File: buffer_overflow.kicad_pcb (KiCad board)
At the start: 2 copper layers, 52 x 107 mm, 27 parts, among them J1 Barrel_Jack_Switch, J3 NRJ4HF, J4 NRJ4HF, U1 LM741

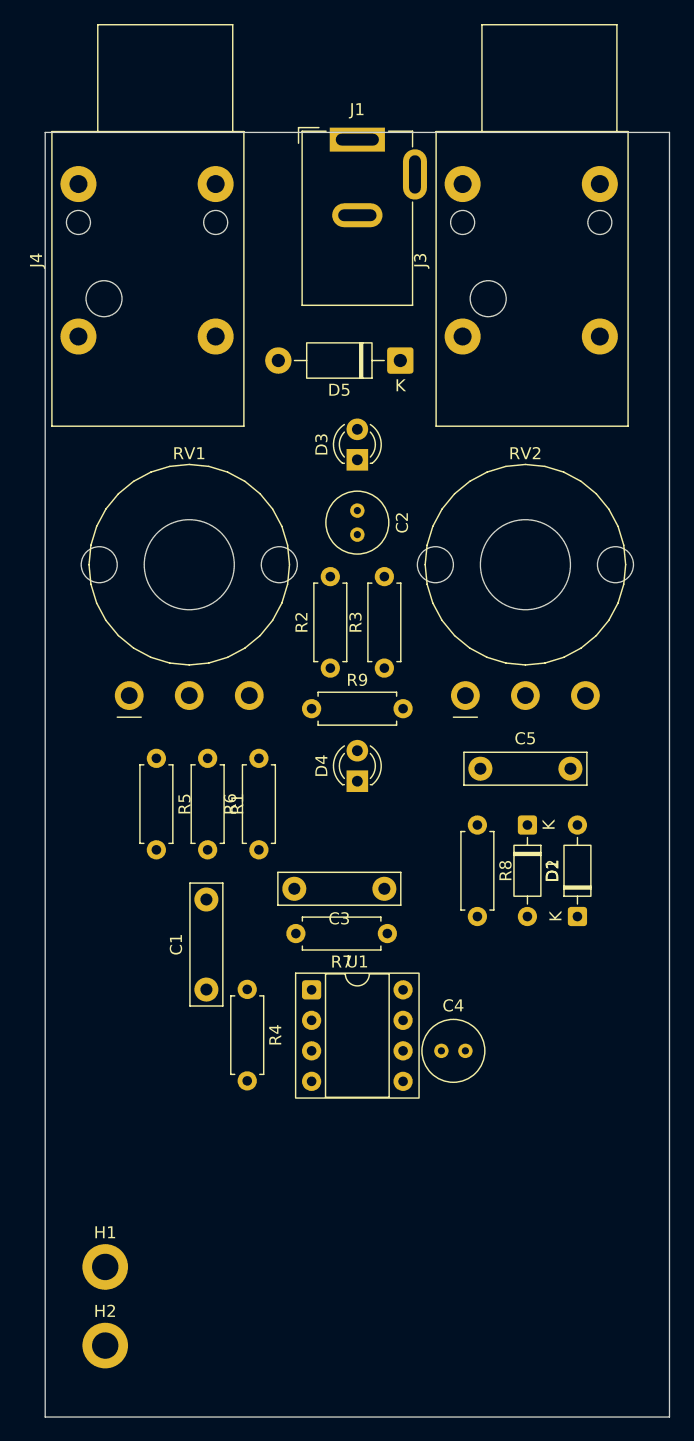
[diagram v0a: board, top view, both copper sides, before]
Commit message: Add Power/LED netclasses and update board
Net classes (Board Setup):
- Power (32 mil): /9V0, /AGND, /PGND, /BAT_GND
- LED (24 mil): /LED*
- Default (14 mil): all other signal nets

Includes accompanying schematic and PCB edits.

Co-Authored-By: Claude Opus 4.8 (1M context) <noreply@anthropic.com>
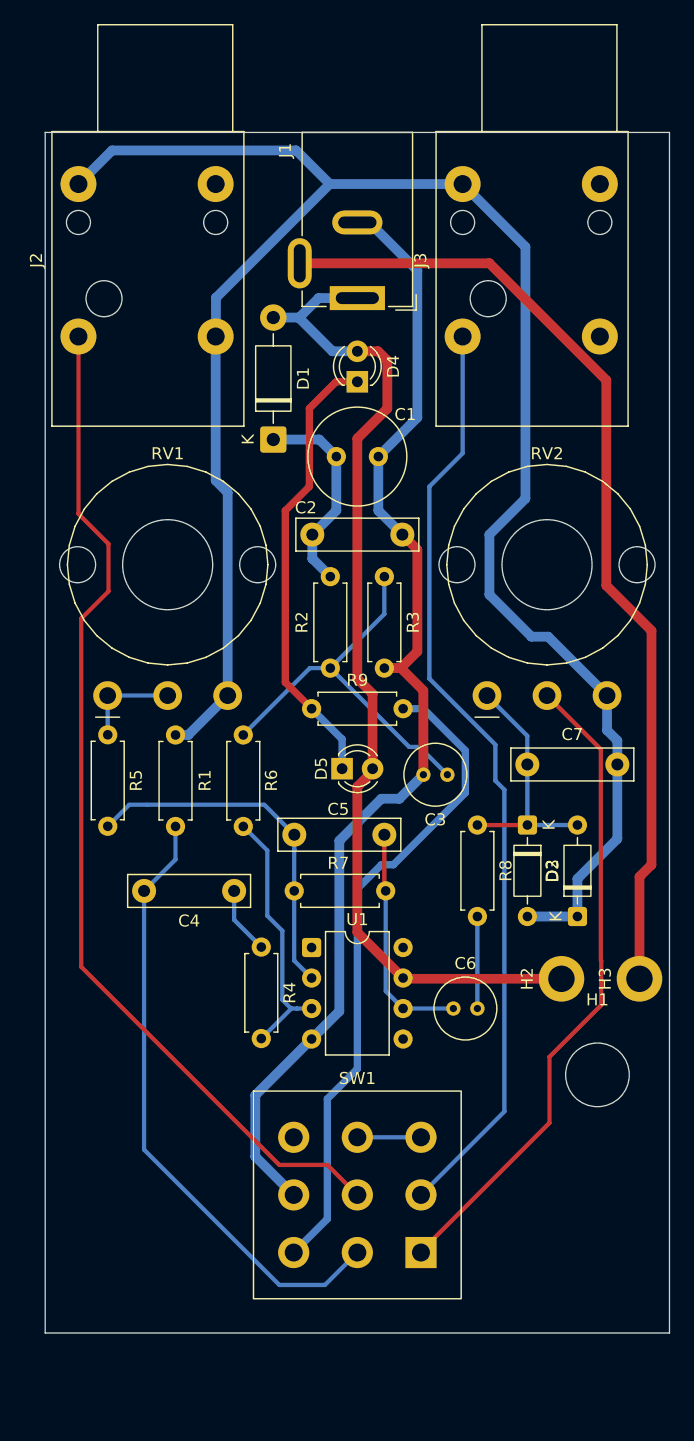
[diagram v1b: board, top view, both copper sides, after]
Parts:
- removed the D5 at (134.1, 78.5)
- added C1: 100uF, Capacitor_THT:C_Radial_D8.0mm_H11.5mm_P3.50mm, F.Cu at (128.8, 86.5)
- added C2: 100nF, Capacitor_THT:C_Rect_L10.0mm_W2.5mm_P7.50mm_MKS4, F.Cu at (126.8, 93.0)
- added D1: 1N4001, Diode_THT:D_DO-41_SOD81_P10.16mm_Horizontal, F.Cu at (123.5, 85.1)
- added H1: MountingHole, MountingHole:MountingHole_5.3mm_M5, F.Cu at (150.5, 138.0)
- added SW1: SW_FSW800_3PDT, edaFactory:SW_FSW800_3PDT, F.Cu at (130.5, 148.0)
- C3: renamed from C2; value C_US -> 10uF
- J2: renamed from J4; value NRJ4HF -> NRJ4HF-1
- U1: value LM741 -> TL071; footprint Package_DIP:DIP-8_W7.62mm_Socket -> Package_DIP:DIP-8_W7.62mm
- moved H3 54.0 mm to (154.0, 130.0), turned to 90 degrees
- moved H2 44.9 mm to (147.5, 130.0), turned to 90 degrees
- moved C3 23.2 mm to (138.0, 113.0), turned to 180 degrees
- moved J1 13.2 mm to (130.5, 73.3), turned to 180 degrees
- moved C4 8.53 mm to (120.2, 122.7), turned to 180 degrees
- moved D4 6.50 mm to (130.5, 80.3)
- moved R5 4.50 mm to (109.7, 109.7)
- moved C5 4.50 mm to (132.8, 118.0)
- moved C7 3.92 mm to (144.7, 112.1)
- moved R4 3.71 mm to (122.5, 127.4)
- moved C6 3.66 mm to (138.5, 132.5)
- moved R7 3.56 mm to (132.9, 122.7)
- moved U1 3.52 mm to (126.7, 127.4)
- moved R1 3.31 mm to (115.4, 109.7)
- moved R6 2.34 mm to (121.0, 117.3)
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- renumbered C1 to C4, C3 to C5, C4 to C6, C5 to C7, D1 to D2, D2 to D3, D3 to D4, D4 to D5, H1 to H2, H2 to H3
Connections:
- net /741_Inv renamed /INV
- net /741_OUT renamed /OPAMPOUT
- net Net-(H2-Pad1) renamed /BAT_GND
- net Net-(U1-+) renamed /NINV
- C4 pad 2: /EFFECT_IN -> /CIRCIN
- D4 pad 1: unconnected-(D3-K-Pad1) -> /LEDK
- D4 pad 2: Net-(D3-A) -> /9V0
- D5 pad 1: unconnected-(D4-K-Pad1) -> /LEDK
- D5 pad 2: unconnected-(D4-A-Pad2) -> /9V0
- J2 pad S: /EFFECT_IN -> /AGND
- J2 pad SN: /AGND -> unconnected-(J2-PadSN)
- J2 pad T: /AGND -> /INPUT_TIP
- J2 pad TN: unconnected-(J4-PadTN) -> /AGND
- J3 pad S: /EFFECT_OUT -> /AGND
- J3 pad T: /AGND -> /OUT_TIP
- R1 pad 2: /EFFECT_IN -> /CIRCIN
- R9 pad 1: unconnected-(R9-Pad1) -> /LEDK
- R9 pad 2: Net-(D3-A) -> /LEDA
- RV2 pad 2: /EFFECT_OUT -> /CIRCOUT
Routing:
- net /AGND: track 0.00 -> 162.2 mm
- net /PGND: track 0.00 -> 97.1 mm
- net /INPUT_TIP: track 0.00 -> 85.3 mm
- net /9V0: track 0.00 -> 84.8 mm
- net /BAT_GND: track 0.00 -> 81.4 mm
- net /OUT_TIP: track 0.00 -> 78.1 mm
- net /LEDA: track 0.00 -> 54.9 mm
- net /CIRCOUT: track 0.00 -> 54.5 mm
- net /CIRCIN: track 0.00 -> 51.6 mm
- net /LEDK: track 0.00 -> 37.7 mm
- net /VREF: track 0.00 -> 32.5 mm
- net /INV: track 0.00 -> 28.9 mm
- net /NINV: track 0.00 -> 22.1 mm
- net /PRE_VOLUME: track 0.00 -> 20.5 mm
- net /OPAMPOUT: track 0.00 -> 19.3 mm
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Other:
- board size 52 x 107 mm -> 52 x 100 mm

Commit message: Add /VREF to Power netclass and route board
Co-Authored-By: Claude Opus 4.8 (1M context) <noreply@anthropic.com>
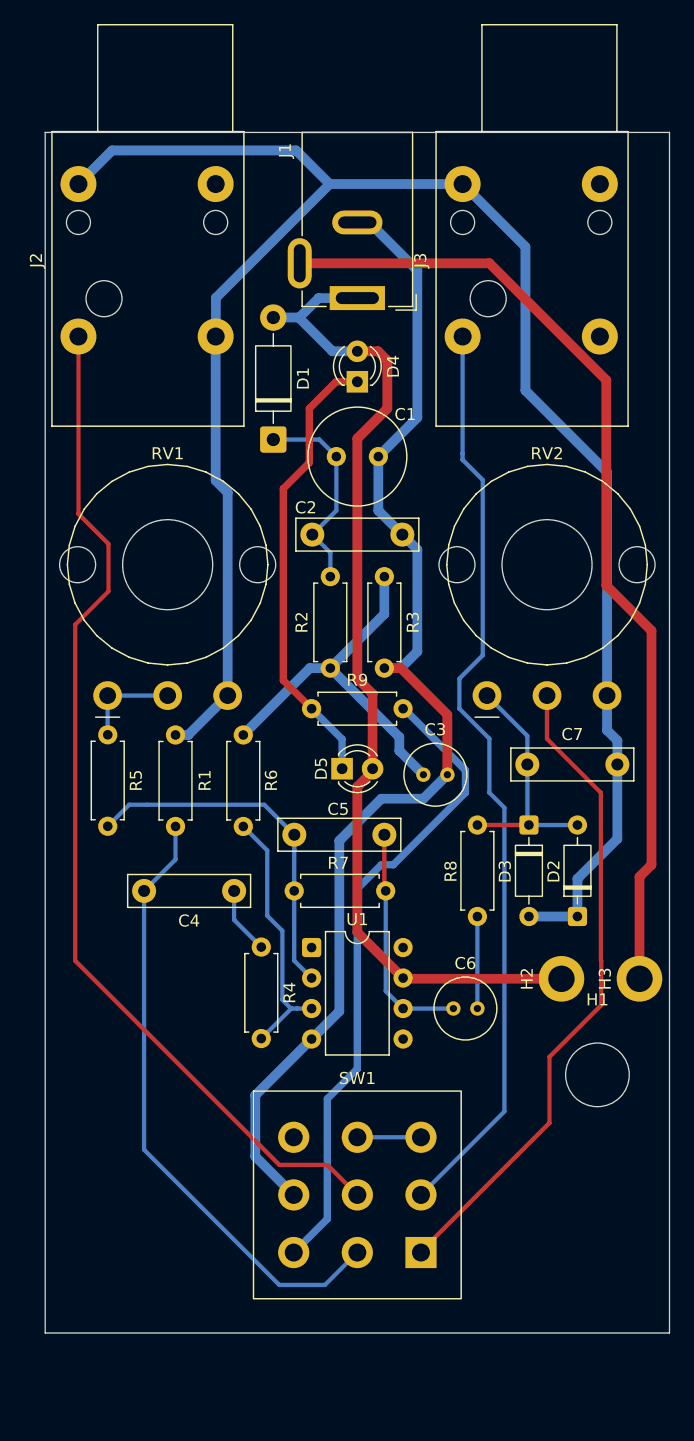
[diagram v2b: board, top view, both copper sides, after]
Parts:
- moved C3 2.00 mm to (136.0, 113.0), turned to 0 degrees
- moved D3 0.13 mm to (144.8, 117.2)
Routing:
- net /PGND: track 97.1 -> 101.3 mm
- net /AGND: track 162.2 -> 158.7 mm
- net /VREF: track 32.5 -> 31.1 mm
- net /LEDA: track 54.9 -> 54.0 mm
- net /OUT_TIP: track 78.1 -> 77.4 mm

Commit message: Add back-silkscreen contact/credit text
Co-Authored-By: Claude Opus 4.8 (1M context) <noreply@anthropic.com>
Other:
- board text added: "DAVID SHUMAN"
- board text added: "DOD OD-250"
- board text added: "davidshuman@gmail.com hardware & software analog - digital - audio tube amplifiers"

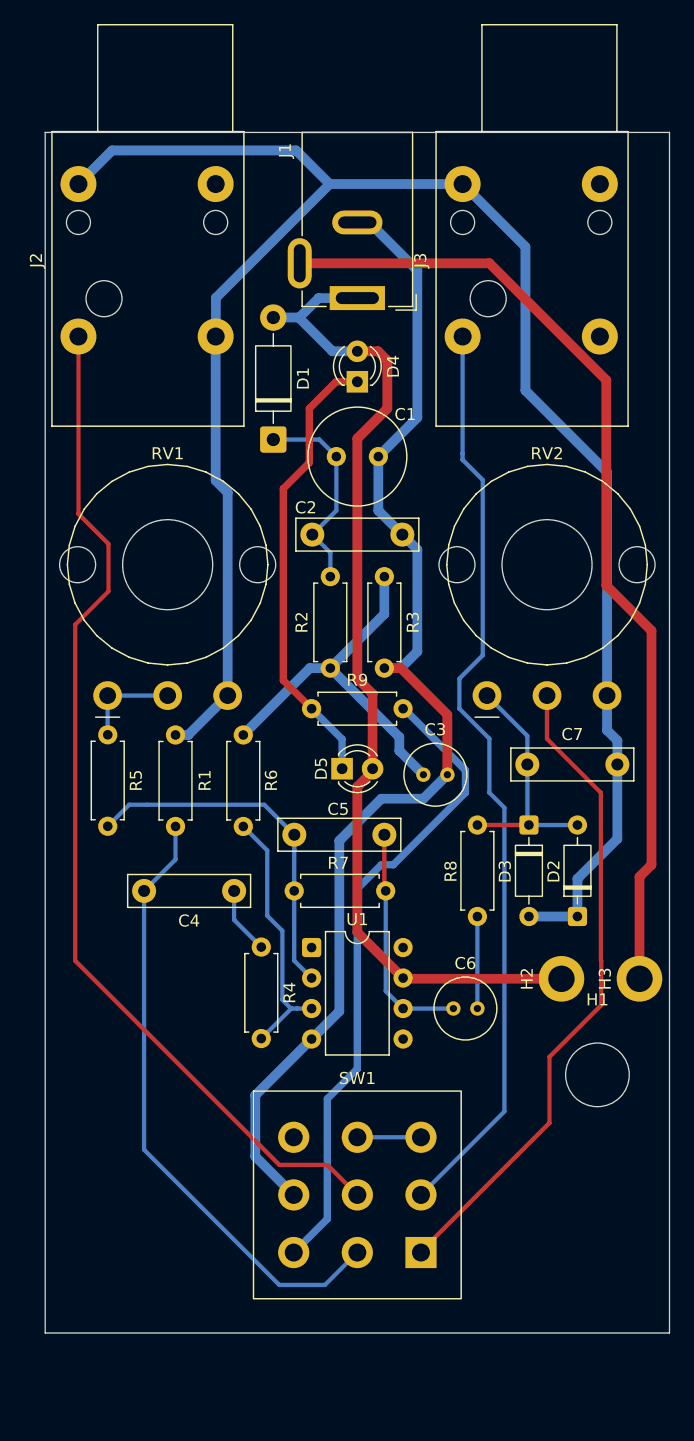
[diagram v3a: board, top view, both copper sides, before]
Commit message: Add logo, battery terminals, and silkscreen labels
Co-Authored-By: Claude Opus 4.8 (1M context) <noreply@anthropic.com>
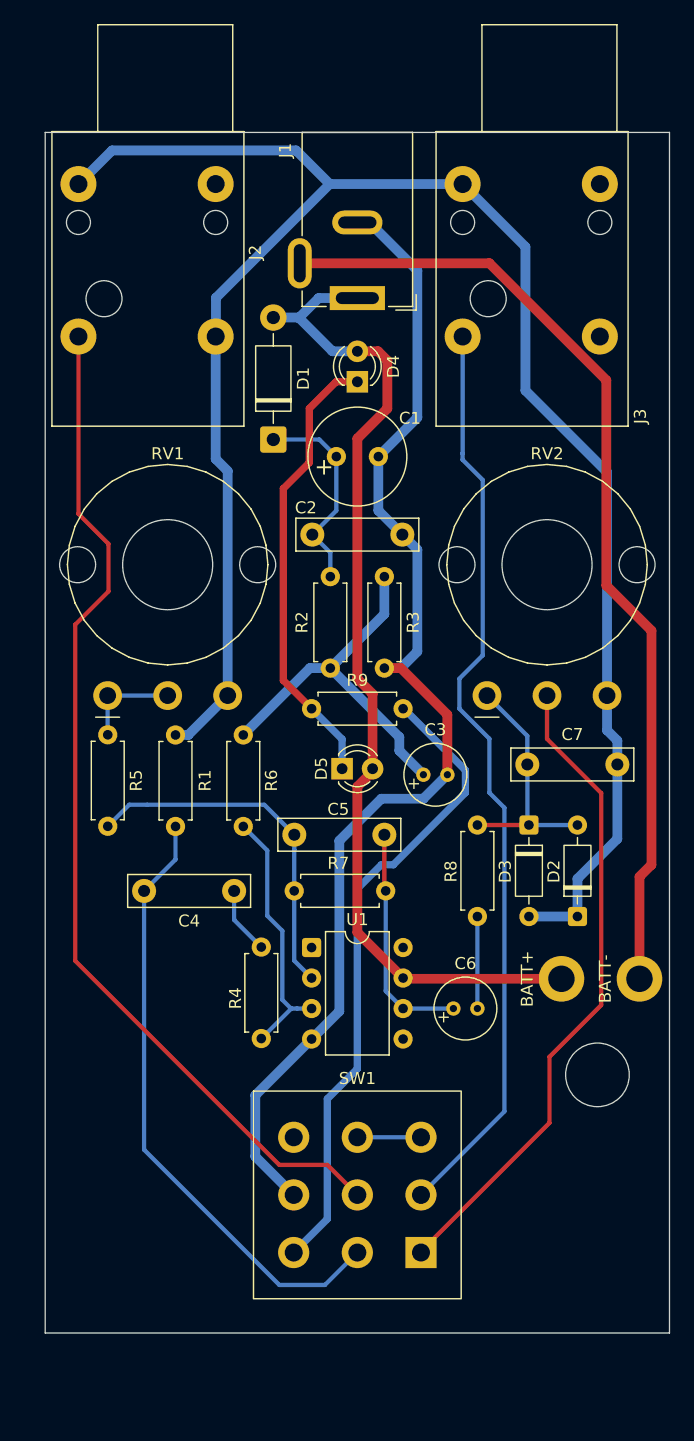
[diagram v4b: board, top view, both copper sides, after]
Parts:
- added G***: LOGO, LOGO, B.Cu at (147.0, 150.0)
- renumbered H2 to BATT+, H3 to BATT-
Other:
- board text added: "+"
- board text added: "DOD OD PREAMP 250"
- board text added: "davidshuman@gmail.com hardware - firmware analog - digital - audio tube amplifiers"
- board text removed: "DOD OD-250"
- board text removed: "davidshuman@gmail.com hardware & software analog - digital - audio tube amplifiers"
